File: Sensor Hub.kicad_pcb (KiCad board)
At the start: 2 copper layers, 93.1 x 48.9 mm, 72 parts, among them J1 SWD, J2 SD_Card, J3 Screw_Terminal_01x02, J4 USB_B_Micro, Q1 AO3401A, Q2 AO3401A, Q3 AO3401A, SW1 SW_SPDT, SW2 SW_Push, U1 LM20BIM7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

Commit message: Rev 1.0
+ Initial PCB board completed
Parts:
- C21, C23, D3, L1, Q3, R18, R19: moved to F.Cu
- U5: footprint Connector_PinSocket_2.00mm:PinSocket_1x04_P2.00mm_Horizontal -> Connector_PinSocket_2.00mm:PinSocket_1x04_P2.00mm_Vertical
- moved R8 135.3 mm to (178.6, 49.6)
- moved R6 127.9 mm to (172.0, 47.8), turned to 90 degrees
- moved R7 127.2 mm to (172.0, 51.9), turned to -90 degrees
- moved U7 126.1 mm to (174.7, 49.1), turned to 90 degrees
- moved C19 125.3 mm to (178.6, 47.3), turned to 180 degrees
- moved C20 123.3 mm to (177.5, 52.5), turned to 180 degrees
- moved C16 120.0 mm to (197.2, 44.1)
- moved R5 115.3 mm to (174.2, 53.4), turned to -90 degrees
- moved C17 112.3 mm to (175.9, 62.1), turned to 90 degrees
- moved U4 110.2 mm to (140.6, 60.9), turned to 180 degrees
- moved C18 109.4 mm to (170.9, 56.6), turned to 45 degrees
- moved U1 107.6 mm to (175.0, 58.5)
- moved C2 107.0 mm to (147.1, 51.6), turned to 90 degrees
- moved C23 106.0 mm to (133.3, 65.2), turned to 0 degrees
- moved L1 103.3 mm to (129.0, 62.6), turned to 0 degrees
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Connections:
- J2 pad CP: (no net) -> GND
- J2 pad SH: (no net) -> GND
- J2 pad SW: (no net) -> GND
- J2 pad WP: (no net) -> GND
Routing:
- net GND: track 52.7 -> 165.7 mm, vias 6 -> 37
- net +3V3: track 65.9 -> 160.8 mm, vias 3 -> 0
- net SPI1_MOSI: track 0.00 -> 50.0 mm, vias 0 -> 2
- net /Power/BAT-: track 0.00 -> 48.9 mm, vias 0 -> 1
- net CS#: track 0.00 -> 47.0 mm, vias 0 -> 2
- net USART1_TX: track 0.00 -> 41.9 mm, vias 0 -> 2
- net SPI1_CLK: track 0.00 -> 39.1 mm, vias 0 -> 2
- net /Power/BAT+: track 37.9 -> 1.52 mm, vias 1 -> 0
- net SPI1_MISO: track 0.00 -> 36.2 mm, vias 0 -> 2
- net USART1_RX: track 0.00 -> 35.6 mm, vias 0 -> 2
- net SPI1_IRQ: track 0.00 -> 23.6 mm, vias 0 -> 2
- net I2C2_CLK: track 0.00 -> 19.5 mm, vias 0 -> 2
- net I2C2_SDA: track 0.00 -> 14.6 mm, vias 0 -> 2
- net BOOT0: track 3.54 -> 17.9 mm
- net Net-(Q2-D): track 0.00 -> 14.2 mm
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- added copper zone on F.Cu, net +3V3
- added copper zone on F.Cu, net /Power/BAT+
- added copper zone on B.Cu, net GND
- added copper zone on F.Cu, net GND
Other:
- board size 93.1 x 48.9 mm -> 107.9 x 36.1 mm

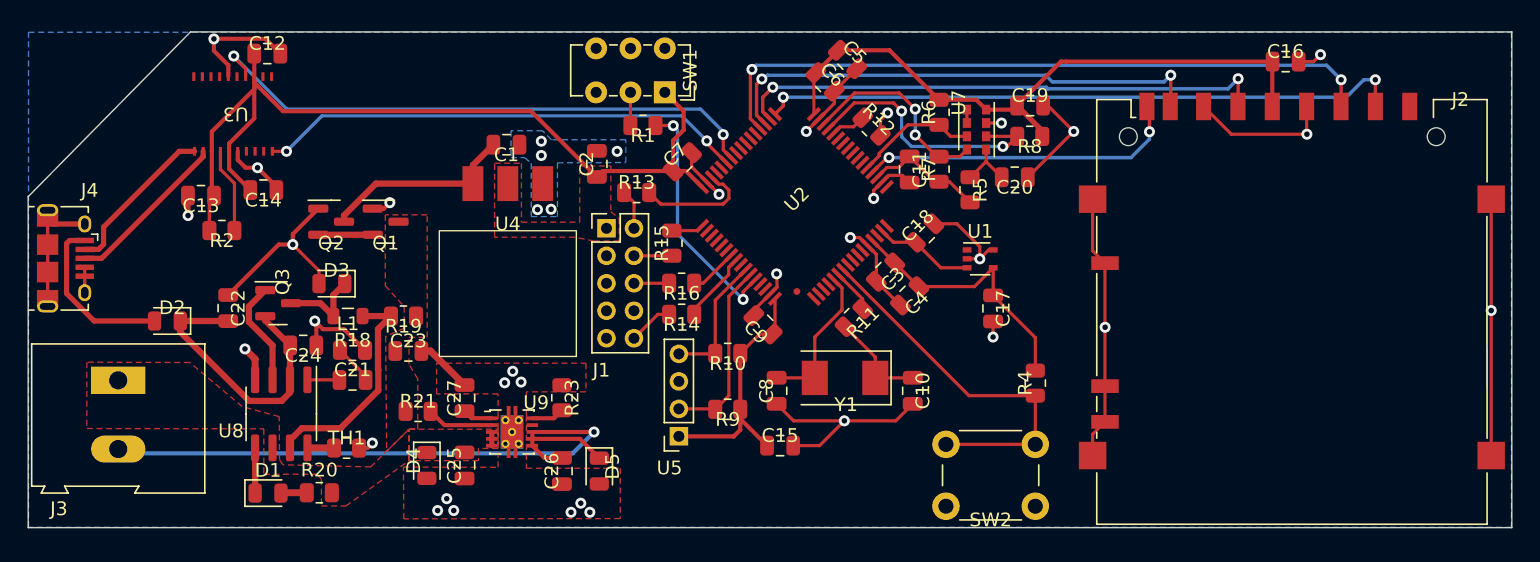
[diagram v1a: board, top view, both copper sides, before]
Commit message: Updated to Rev 1.1
+ Adjusted trace widths to appropriately fit IC pads while supporting wanted current and minimizing vdrop
+ Adjusted edge cuts of PCB to remove unnecessary areas
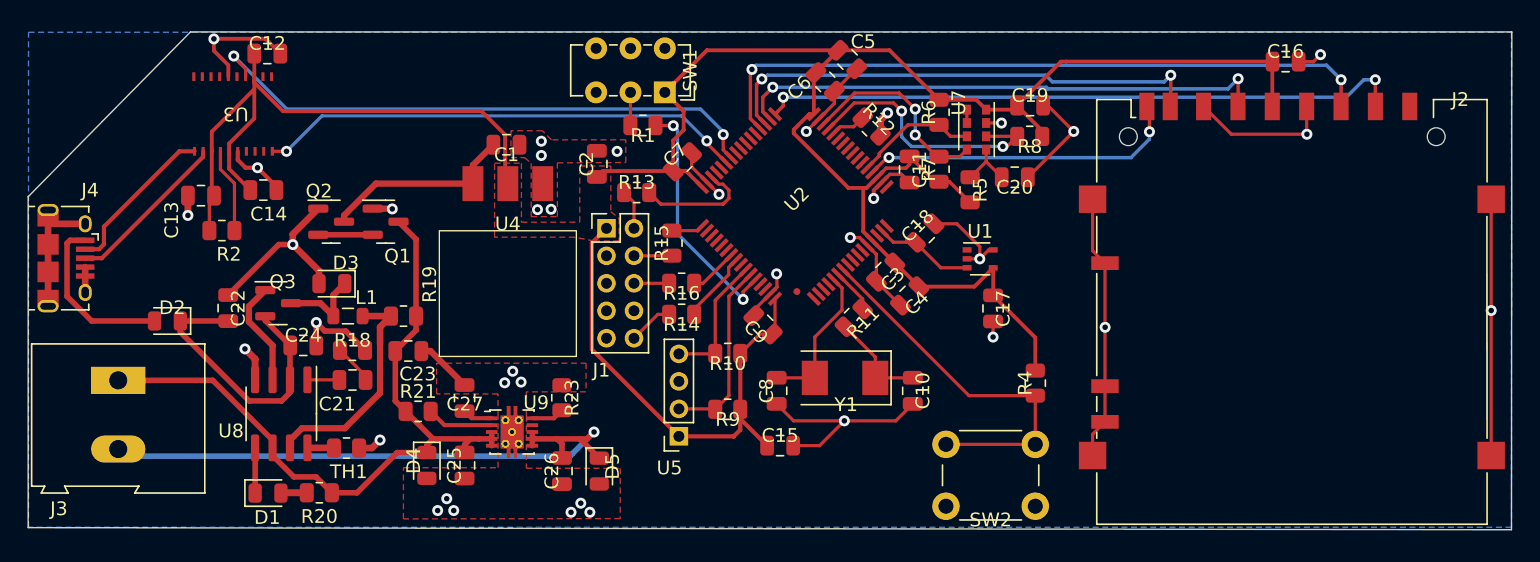
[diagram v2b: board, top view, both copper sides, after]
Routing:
- net /Power/BAT+: track 1.52 -> 53.4 mm
- net +3V3: track 160.8 -> 203.0 mm
- net /Power/BAT-: track 48.9 -> 44.7 mm
- removed copper zone on F.Cu, net /Power/BAT+
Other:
- board size 107.9 x 36.1 mm -> 107.9 x 36.2 mm

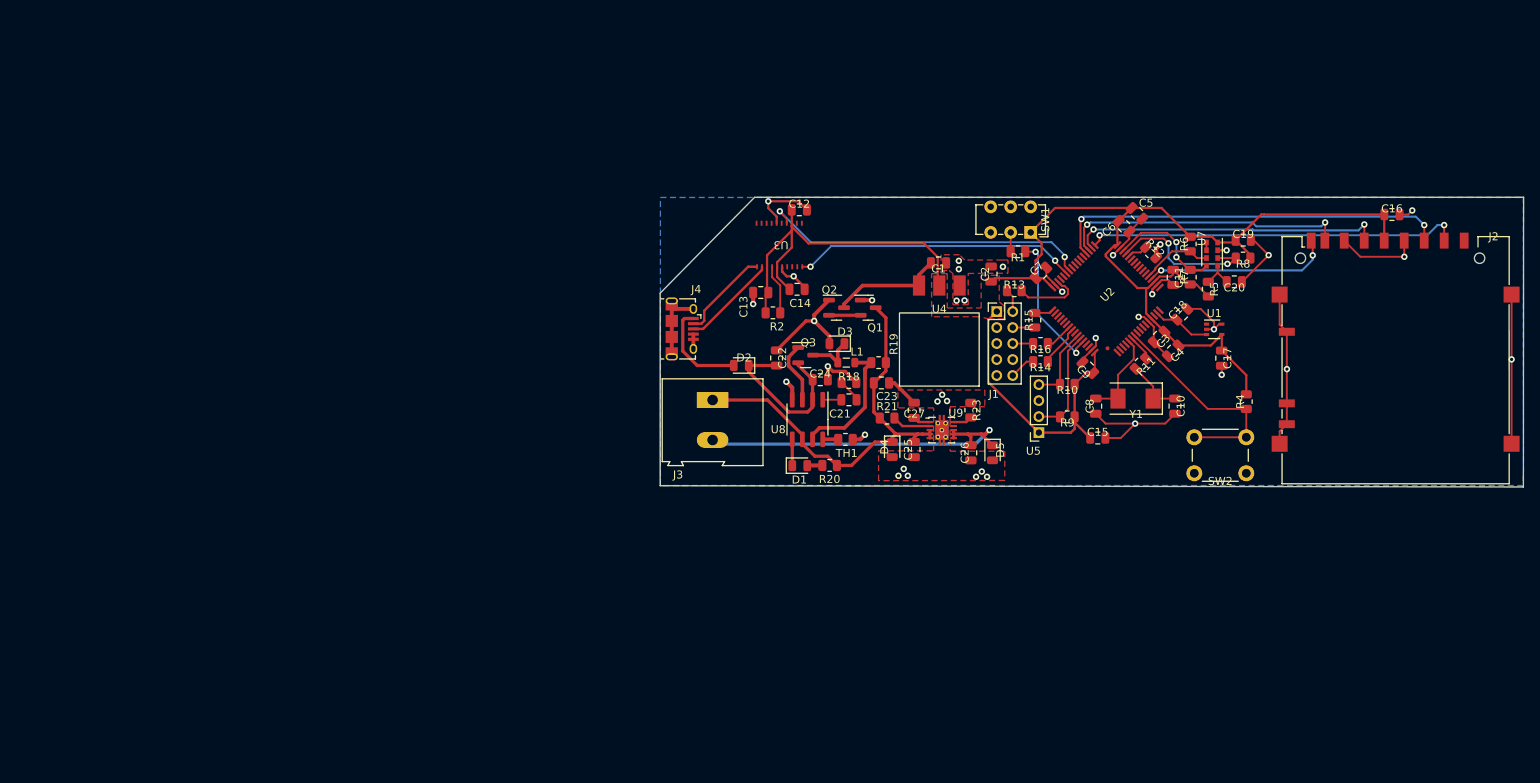
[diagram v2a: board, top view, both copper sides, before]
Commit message: Updated Rev 2.0
+ Revamped board to 4 layer with components on both signal layers (top/bottom)
+ Adjusted compactness of components, reducing size by approx 30%
+ Added mounting holes for mounting purposes
- Removed battery, batt charger, eFuse (USB driven only)
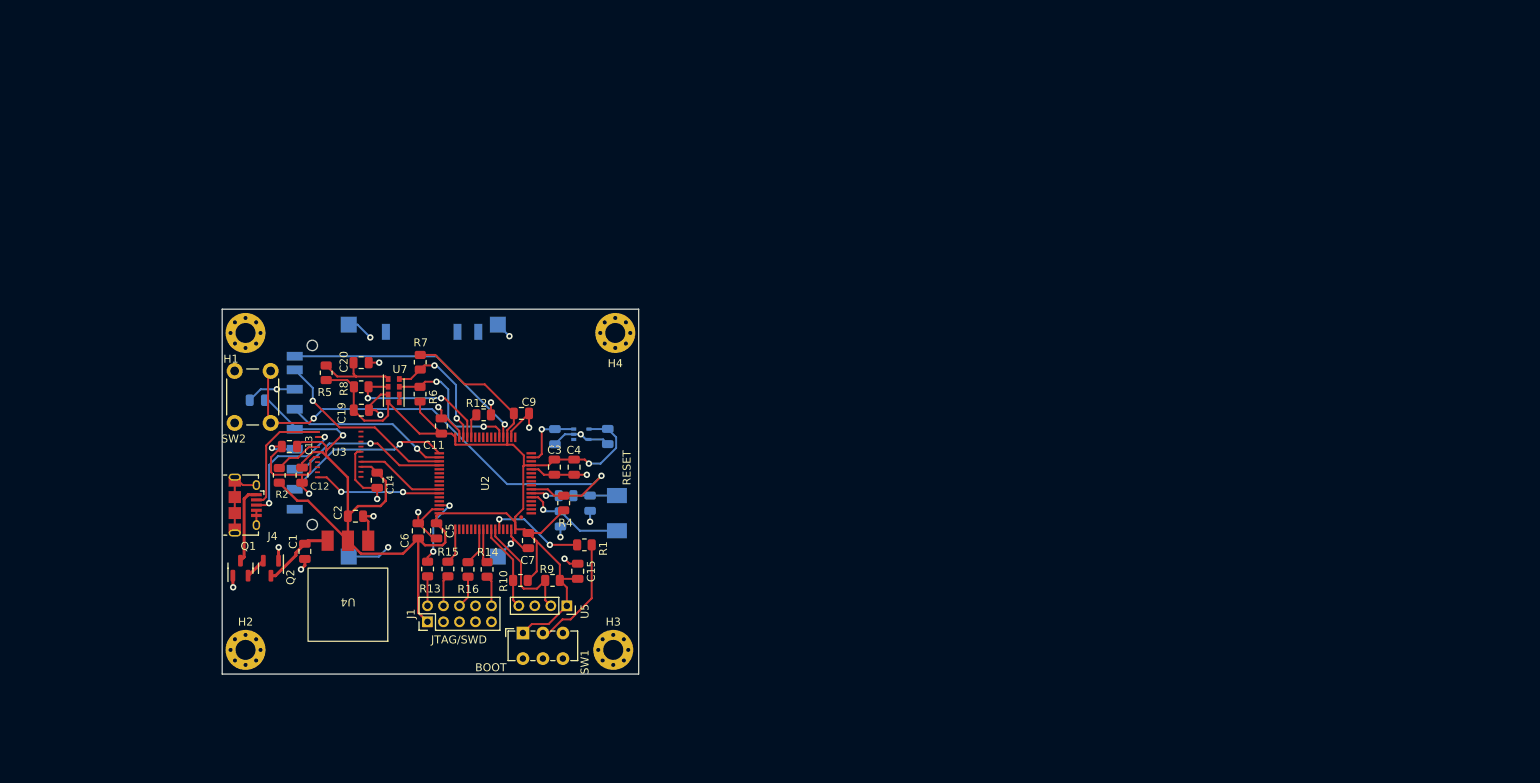
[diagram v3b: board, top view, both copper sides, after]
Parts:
- removed C21: 0.47uF, Capacitor_SMD:C_0805_2012Metric
- removed C22: 10uF, Capacitor_SMD:C_0805_2012Metric
- removed C23: 22uF, Capacitor_SMD:C_0805_2012Metric
- removed C24, C25: 0.1uF, Capacitor_SMD:C_0805_2012Metric
- removed C26: 1uF, Capacitor_SMD:C_0805_2012Metric
- removed C27: 1nF, Capacitor_SMD:C_0805_2012Metric
- removed D1: LED, LED_SMD:LED_0805_2012Metric
- removed D2, D3, D4, D5: D_Schottky, Diode_SMD:D_0805_2012Metric
- removed J3: Screw_Terminal_01x02, TerminalBlock:TerminalBlock_Altech_AK300-2_P5.00mm
- removed L1: 6.8 uH, Inductor_SMD:L_0805_2012Metric
- removed Q3: AO3401A, Package_TO_SOT_SMD:SOT-23
- removed R18: 2.2k, Resistor_SMD:R_0805_2012Metric
- removed R19: 68m, Resistor_SMD:R_0805_2012Metric
- removed R20: 2k, Resistor_SMD:R_0805_2012Metric
- removed R21: 1M, Resistor_SMD:R_0805_2012Metric
- removed R23: 100K, Resistor_SMD:R_0805_2012Metric
- removed TH1: 10k, Resistor_SMD:R_0805_2012Metric
- removed U8: LTC4002ES8-4.2, Package_SO:SOIC-8_3.9x4.9mm_P1.27mm
- removed U9: TPS2592xx, Package_SON:VSON-10-1EP_3x3mm_P0.5mm_EP1.65x2.4mm_ThermalVias
- added H1: MountingHole, MountingHole:MountingHole_2.5mm_Pad_Via, F.Cu at (53.8, 58.9)
- added H2: MountingHole, MountingHole:MountingHole_2.5mm_Pad_Via, F.Cu at (53.8, 98.6)
- added H3: MountingHole, MountingHole:MountingHole_2.5mm_Pad_Via, F.Cu at (99.8, 98.6)
- added H4: MountingHole, MountingHole:MountingHole_2.5mm_Pad_Via, F.Cu at (100.1, 58.9)
- C10, C16, C17, C18, C8, J2, R11, U1, Y1: moved to B.Cu
- moved C16 143.7 mm to (55.3, 67.3), turned to 180 degrees
- moved J2 123.1 mm to (74.9, 72.4), turned to -90 degrees
- moved SW2 115.8 mm to (57.0, 63.7), turned to -90 degrees
- moved C19 112.3 mm to (68.3, 68.6)
- moved R8 111.4 mm to (68.3, 65.7), turned to 180 degrees
- moved R5 110.8 mm to (63.9, 63.9)
- moved C20 109.6 mm to (68.3, 62.6)
- moved U7 103.7 mm to (72.4, 66.1), turned to -90 degrees
- moved R6 98.1 mm to (75.7, 66.6), turned to -90 degrees
- moved R7 96.9 mm to (75.7, 62.6), turned to 90 degrees
- moved C5 96.2 mm to (77.7, 83.7), turned to -90 degrees
- moved C6 96.1 mm to (75.4, 83.7), turned to 90 degrees
- moved C11 93.4 mm to (78.3, 70.6), turned to 90 degrees
- moved C1 87.0 mm to (61.3, 86.2), turned to -90 degrees
- moved R4 86.3 mm to (93.6, 80.2), turned to 90 degrees
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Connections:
- J2 pad CP: GND -> (no net)
- J2 pad SW: GND -> (no net)
- J2 pad WP: GND -> (no net)
- Q1 pad 3: /Power/BAT+ -> +5V
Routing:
- net /Power/BAT+: track 53.4 -> 0.00 mm
- net GND: track 165.5 -> 118.8 mm, vias 37 -> 23
- net /Power/BAT-: track 44.7 -> 0.00 mm, vias 1 -> 0
- net NRST: track 27.8 -> 63.3 mm, vias 0 -> 2
- net USART1_TX: track 41.9 -> 11.2 mm, vias 2 -> 0
- net SPI1_MOSI: track 50.0 -> 20.5 mm, vias 2 -> 1
- net CS#: track 47.0 -> 21.1 mm, vias 2 -> 1
- net Net-(D2-K): track 20.9 -> 0.00 mm
- net USART1_RX: track 35.6 -> 16.1 mm
- net SPI1_CLK: track 39.1 -> 20.6 mm, vias 2 -> 1
- net +3V3: track 203.0 -> 219.8 mm, vias 0 -> 2
- net Net-(U8-SENSE): track 16.5 -> 0.00 mm
- net SPI1_MISO: track 36.2 -> 23.8 mm, vias 2 -> 1
- net Net-(SW1-B): track 2.42 -> 14.6 mm
- net I2C2_IRQ: track 8.97 -> 18.4 mm, vias 0 -> 2
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- added copper zone on In1.Cu, net GND
- added copper zone on In2.Cu, net GND
- removed copper zone on F.Cu, net +3V3
- removed copper zone on B.Cu, net GND
- removed copper zone on F.Cu, net GND
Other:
- board size 107.9 x 36.2 mm -> 52.1 x 45.6 mm
- copper layers 2 -> 4
- board text added: "BOOT"
- board text added: "JTAG/SWD"
- board text added: "RESET"
